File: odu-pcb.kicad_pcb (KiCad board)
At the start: 2 copper layers, 127 x 81.3 mm, 14 parts, among them U1 HCMS, U10 HCMS, U2 HCMS, U3 HCMS, U4 HCMS, U5 HCMS, U6 HCMS, U7 HCMS, U8 HCMS, U9 HCMS

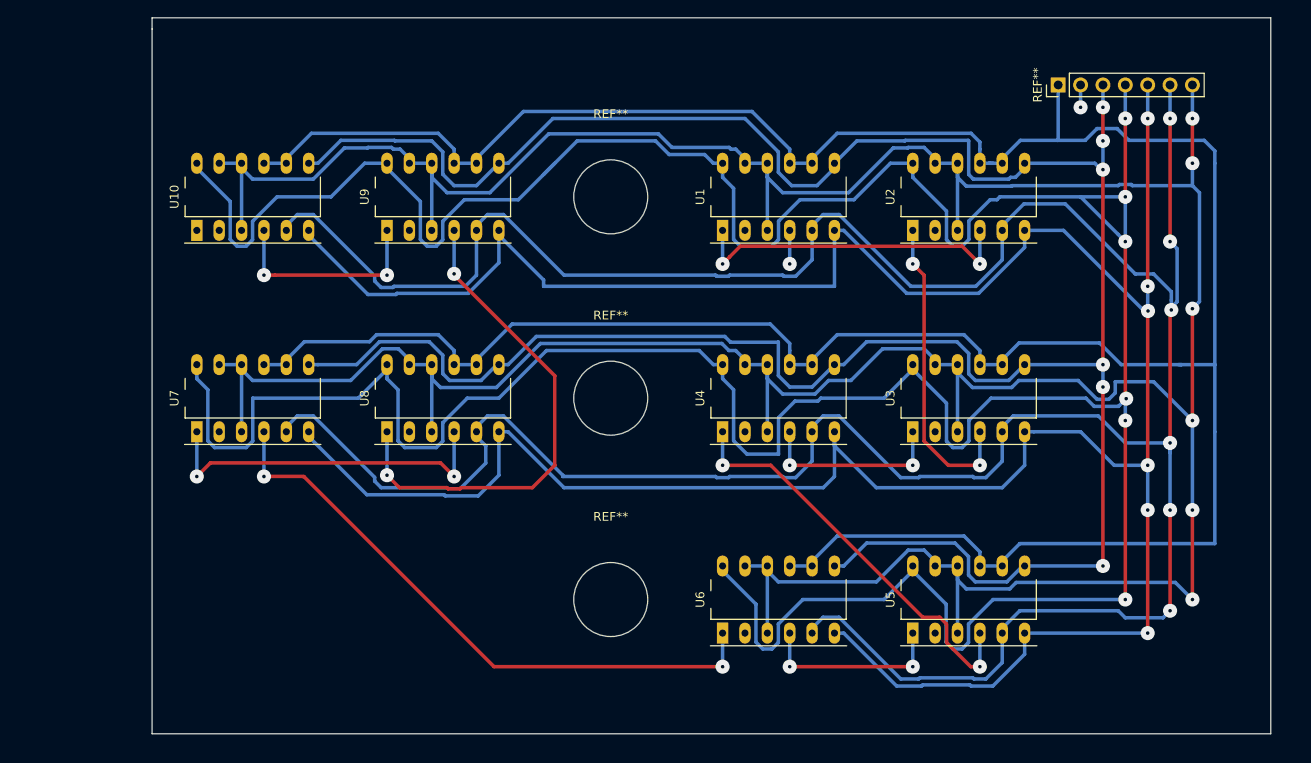
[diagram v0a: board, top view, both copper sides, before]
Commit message: Revision 2: Buttons, no airwires (uses stripboard with two trace cuts as back side
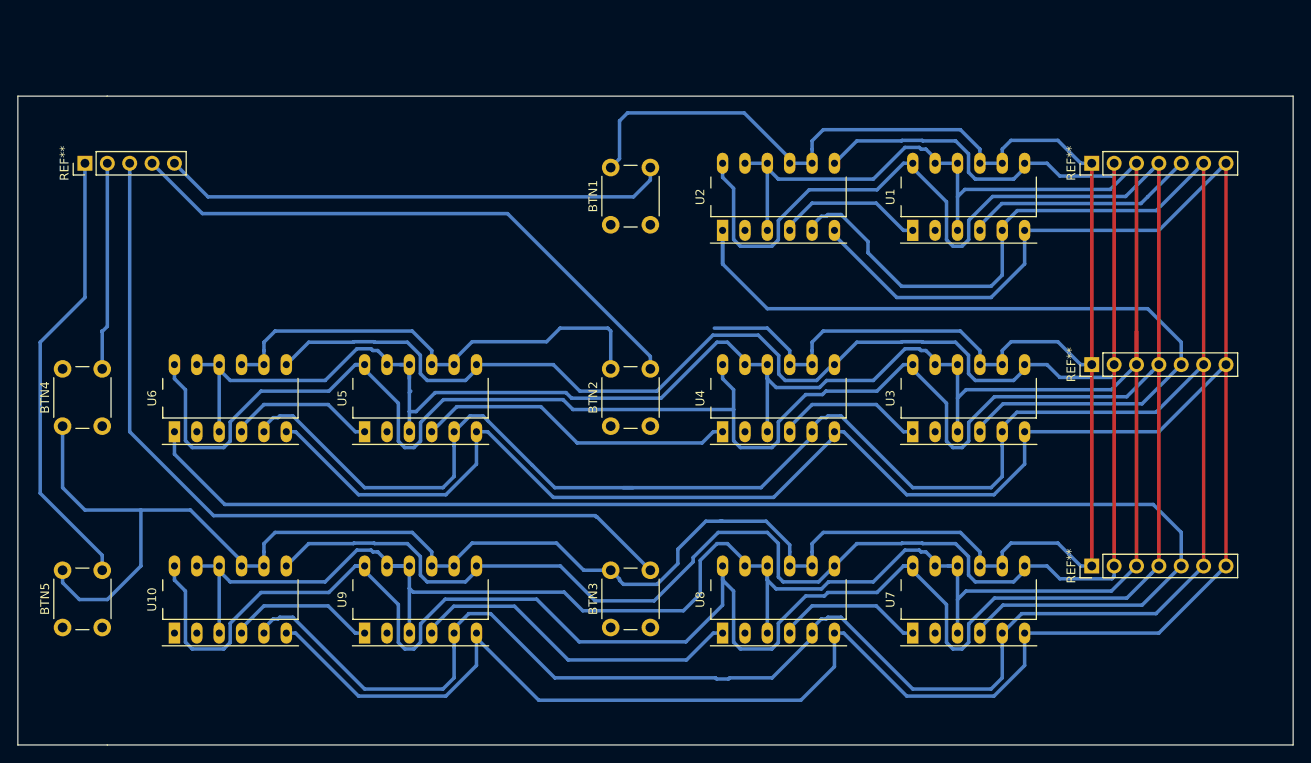
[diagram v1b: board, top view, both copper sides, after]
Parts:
- removed the REF** at (185.4, 29.2)
- removed the REF** at (134.6, 87.6)
- removed the REF** at (134.6, 64.8)
- removed the REF** at (134.6, 41.9)
- added BTN1: SW_Push, odu-pcb:SW_PUSH_6mm_h4.3mm, F.Cu at (134.6, 45.1)
- added BTN2: SW_Push, odu-pcb:SW_PUSH_6mm_h4.3mm, F.Cu at (134.6, 67.9)
- added BTN3: SW_Push, odu-pcb:SW_PUSH_6mm_h4.3mm, F.Cu at (134.6, 90.8)
- added BTN4: SW_Push, odu-pcb:SW_PUSH_6mm_h4.3mm, F.Cu at (72.4, 67.9)
- added BTN5: SW_Push, odu-pcb:SW_PUSH_6mm_h4.3mm, F.Cu at (72.4, 90.8)
- added REF**: BUTTONS, Pin_Headers:Pin_Header_Straight_1x05_Pitch2.54mm, F.Cu at (74.9, 38.1)
- added REF**: BUS, Pin_Headers:Pin_Header_Straight_1x07_Pitch2.54mm, F.Cu at (189.2, 38.1)
- added REF**: BUS, Pin_Headers:Pin_Header_Straight_1x07_Pitch2.54mm, F.Cu at (189.2, 83.8)
- added REF**: BUS, Pin_Headers:Pin_Header_Straight_1x07_Pitch2.54mm, F.Cu at (189.2, 61.0)
- moved U7 84.4 mm to (175.3, 87.6)
- moved U5 66.3 mm to (113.0, 64.8)
- moved U6 66.3 mm to (91.4, 64.8)
- moved U10 45.8 mm to (91.4, 87.6)
- moved U9 45.8 mm to (113.0, 87.6)
- moved U8 44.4 mm to (153.7, 87.6)
- moved U1 21.6 mm to (175.3, 41.9)
- moved U2 21.6 mm to (153.7, 41.9)
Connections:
- net N$1 renamed DOUTU1_TO_DINU2
- net N$2 renamed DOUTU2_TO_DINU3
- net N$3 renamed DOUTU3_TO_DINU4
- net N$4 renamed DOUTU4_TO_DINU5
- net N$5 renamed DOUTU5_TO_DINU6
- net N$6 renamed DOUTU6_TO_DINU7
- net N$7 renamed DOUTU7_TO_DINU8
- net N$8 renamed DOUTU8_TO_DINU9
- net N$9 renamed DOUTU9_TO_DINU10
- U1 pad 4: (no net) -> DIN_U1
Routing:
- net BTN_3: track 0.00 -> 96.1 mm
- net DOUTU6_TO_DINU7: track 69.9 -> 150.7 mm, vias 2 -> 0
- net BTN_2: track 0.00 -> 67.1 mm
- net BTN_1: track 0.00 -> 57.8 mm, vias 0 -> 1
- net DOUTU2_TO_DINU3: track 35.7 -> 92.8 mm, vias 2 -> 0
- net BTN_5: track 0.00 -> 51.2 mm
- net GND: track 354.8 -> 401.0 mm
- net DIN_U1: track 0.00 -> 26.7 mm
- net DOUTU7_TO_DINU8: track 40.6 -> 16.9 mm, vias 2 -> 0
- net BTN_4: track 0.00 -> 23.7 mm
- net DOUTU1_TO_DINU2: track 38.5 -> 16.9 mm, vias 2 -> 0
- net VCC: track 452.7 -> 432.2 mm, vias 6 -> 0
- net DOUTU8_TO_DINU9: track 57.2 -> 38.4 mm, vias 2 -> 0
- net CLK: track 351.4 -> 369.5 mm, vias 6 -> 0
- net DOUTU4_TO_DINU5: track 47.5 -> 35.6 mm, vias 2 -> 0
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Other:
- board size 127 x 81.3 mm -> 144.8 x 73.7 mm
- net class Default: via_drill 0.4 -> 0.8

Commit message: add netlist, pcb2gcode parameters and enclosure design
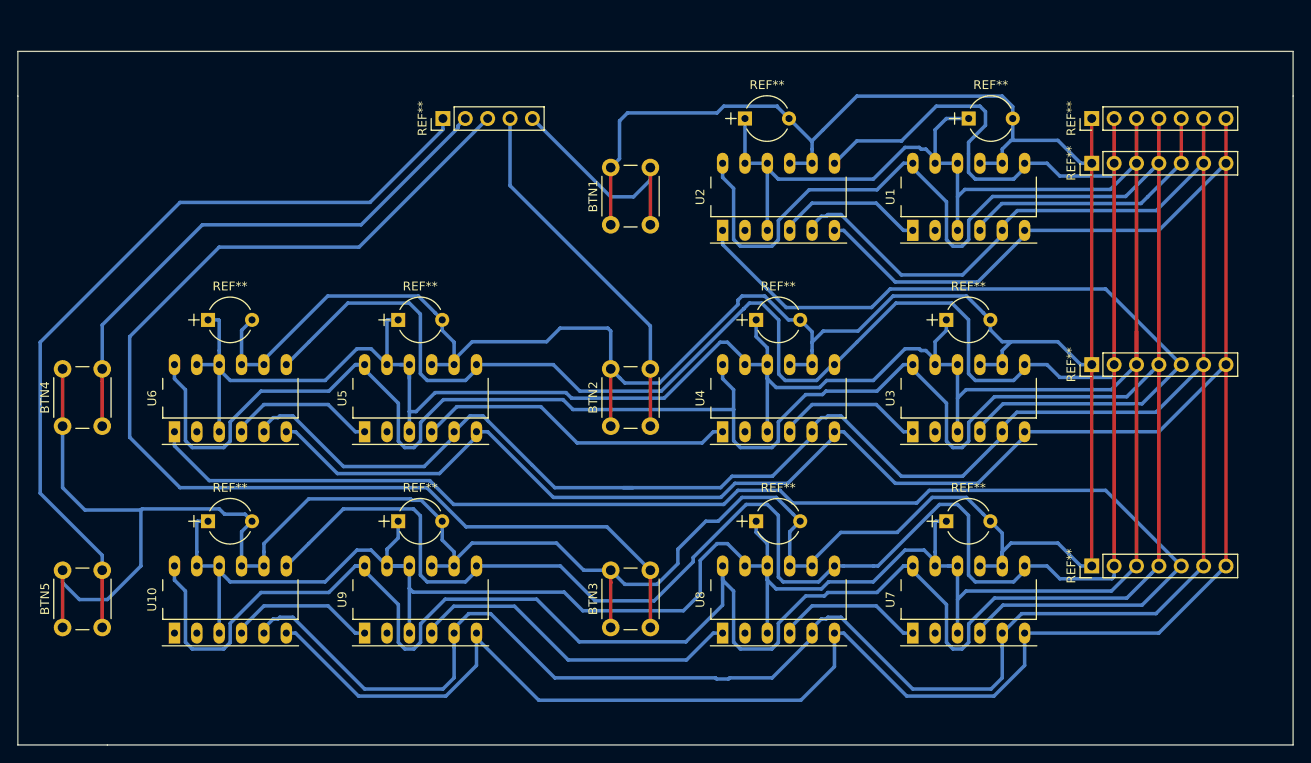
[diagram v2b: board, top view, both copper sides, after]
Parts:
- added REF**: BUS, Pin_Headers:Pin_Header_Straight_1x07_Pitch2.54mm, F.Cu at (189.2, 33.0)
- added REF**: CAP, Capacitors_THT:CP_Radial_Tantal_D5.0mm_P5.00mm, F.Cu at (110.5, 55.9)
- added REF**: CAP, Capacitors_THT:CP_Radial_Tantal_D5.0mm_P5.00mm, F.Cu at (88.9, 55.9)
- added REF**: CAP, Capacitors_THT:CP_Radial_Tantal_D5.0mm_P5.00mm, F.Cu at (172.7, 78.7)
- added REF**: CAP, Capacitors_THT:CP_Radial_Tantal_D5.0mm_P5.00mm, F.Cu at (151.1, 78.7)
- added REF**: CAP, Capacitors_THT:CP_Radial_Tantal_D5.0mm_P5.00mm, F.Cu at (110.5, 78.7)
- added REF**: CAP, Capacitors_THT:CP_Radial_Tantal_D5.0mm_P5.00mm, F.Cu at (88.9, 78.7)
- added REF**: CAP, Capacitors_THT:CP_Radial_Tantal_D5.0mm_P5.00mm, F.Cu at (149.9, 33.0)
- added REF**: CAP, Capacitors_THT:CP_Radial_Tantal_D5.0mm_P5.00mm, F.Cu at (175.3, 33.0)
- added REF**: CAP, Capacitors_THT:CP_Radial_Tantal_D5.0mm_P5.00mm, F.Cu at (172.7, 55.9)
- added REF**: CAP, Capacitors_THT:CP_Radial_Tantal_D5.0mm_P5.00mm, F.Cu at (151.1, 55.9)
- moved REF** 41.0 mm to (115.6, 33.0)
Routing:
- net GND: track 401.0 -> 506.3 mm
- net VCC: track 432.2 -> 497.9 mm
- net CE: track 317.2 -> 365.5 mm
- net BTN_5: track 51.2 -> 92.3 mm
- net BTN_4: track 23.7 -> 62.6 mm
- net BTN_3: track 96.1 -> 134.2 mm
- net BTN_1: track 57.8 -> 25.8 mm
- net BTN_2: track 67.1 -> 41.5 mm
- net RS: track 380.7 -> 373.0 mm
- net CLK: track 369.5 -> 364.2 mm
- net RESET: track 455.7 -> 460.7 mm
- net DIN_U1: track 26.7 -> 31.8 mm
- net DOUTU2_TO_DINU3: track 92.8 -> 88.0 mm
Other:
- board size 144.8 x 73.7 mm -> 144.8 x 78.7 mm
